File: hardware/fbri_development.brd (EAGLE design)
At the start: 95 parts, among them IC3 TLV70033DCK, J1 AAA_HOLDER, U1 SAM_D20E, U2 SI4060, U3 MAX1947, U4 ANTENOVA_GPS_M10382, U5 S25FS-S, U6 STM32F_48PIN, Y1 8MHz

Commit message: Before trying Direct Tie Tx/Rx
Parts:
- removed J1: AAA_HOLDER, fbri:AAA
- added C19: 4.7µF, resistor:C0603K
- added C27, C28, C29, C30: 10µF, resistor:C0603K
- added C31, C32: 100pF, resistor:C0603K
- added IC1: (no value), SparkFun:SOT223
- added JP16: (no value), SparkFun:1X02_LOCK
- added R22, R23: 1Ω, microbuilder_v3:_0402
- added U$99: INA216, fbri:WCSP-4
- added U7: LP38501TS-ADJ/NOPB, LP38501TS-ADJ:TO170P1435X457-6N
- moved JP14 70.4 mm to (45.5, 38.5), turned to 180 degrees
- moved JP13 64.4 mm to (45.5, 35.5), turned to 180 degrees
- moved JP12 25.8 mm to (45.6, 15.4), turned to 180 degrees
- moved C14 22.8 mm to (44.0, 23.4)
- moved C4 22.8 mm to (44.0, 26.5)
- moved C5 22.8 mm to (44.0, 24.6)
- moved JP2 22.5 mm to (38.5, 27.0)
- moved L1 22.5 mm to (41.1, 24.1)
- moved R5 22.5 mm to (43.5, 20.0)
- moved R6 22.5 mm to (43.5, 19.0)
- moved R7 22.5 mm to (39.5, 29.0)
- moved R8 22.5 mm to (39.5, 30.0)
- moved U$2 22.5 mm to (43.5, 21.0)
- moved U$5 22.5 mm to (39.5, 31.0)
- moved U3 22.5 mm to (41.1, 21.4)
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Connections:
- removed net N$1: U6.10
- removed net N$5: JP1.2, JP13.1, JP14.1, R5.2, R6.2, U$2.A1
- removed net PWR_BR: U6.19
- new net 1.2VREG_OUT: C27.1, IC1.2, IC1.4, JP16.2
- new net ADJ_REG_EN: U6.13, U7.1
- new net ADJ_REG_OUT: C29.1, C30.1, C32.1, JP13.2, U7.4
- new net ADJ_REG_SWITCHING: U6.14, U7.5
- new net I_PA: U$99.B2
- new net I_STEPUP_IN: U$2.B2, U6.16
- new net I_STEPUP_OUT: U$5.B2, U6.19
- new net I_VDD_GPS: U$62.B2, U6.15
- new net I_VDD_MEM: U$48.B2, U6.12
- new net I_VDD_RADIO: U$60.B2, U6.10
- new net I_VDD_SAMD20: U$30.B2, U6.11
- new net VDD_PA: L2.2, R22.1, R23.1, U$99.A2
- new net VDD_STEPUP: JP1.2, JP13.1, JP14.1, JP16.1, R5.2, R6.2, U$2.A1, U6.17
- net 1.2V: no longer J1.+2, JP13.2
- net 1.8V: now also U6.18
- net 3.3V: now also JP14.2; no longer U6.41
- net 5.0V: now also C19.1, C28.1, C31.1, IC1.3, U7.2
- net GND: now also C19.2, C27.2, C28.2, C29.2, C30.2, C31.2, C32.2, IC1.1, U$99.B1, U7.3, U7.6; no longer J1.-1, J1.-2
- net RADIO_VDD: now also R22.2, R23.2, U$99.A1; no longer L2.2
- net RESETN: now also U1.5; no longer U1.15, U1.6
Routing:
- net 1.8V: track 20.4 -> 98.8 mm, vias 0 -> 2
- net 5.0V: track 11.9 -> 81.7 mm
- net I_VDD_RADIO: track 0.00 -> 45.5 mm, vias 0 -> 4
- net VDD_STEPUP: track 0.00 -> 40.1 mm, vias 0 -> 2
- net I_VDD_SAMD20: track 0.00 -> 36.5 mm, vias 0 -> 2
- net ADJ_REG_OUT: track 0.00 -> 35.4 mm, vias 0 -> 1
- net ADJ_REG_EN: track 0.00 -> 35.1 mm
- net ADJ_REG_SWITCHING: track 0.00 -> 28.8 mm
- net RESETN: track 15.9 -> 36.7 mm, vias 0 -> 2
- net TIME_1KHZ: track 6.47 -> 26.9 mm, vias 0 -> 2
- net I_STEPUP_IN: track 0.00 -> 20.2 mm, vias 0 -> 2
- net I_VDD_MEM: track 0.00 -> 16.9 mm
- net I_VDD_GPS: track 0.00 -> 15.2 mm, vias 0 -> 2
- net 1.2VREG_OUT: track 0.00 -> 14.8 mm
- net SWDCLK: track 20.0 -> 6.06 mm
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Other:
- board outline added: 50 x 50 mm
- board text added: "!IRQ"
- board text added: "!SEL"
- board text added: "Board"
- board text added: "Devlopment"
- board text added: "GPS UART"
- board text added: "HFCLK"
- board text added: "Radio SPI"
- board text removed: "HF_CLK"
- board text removed: "NIRQ"
- board text removed: "NSEL"

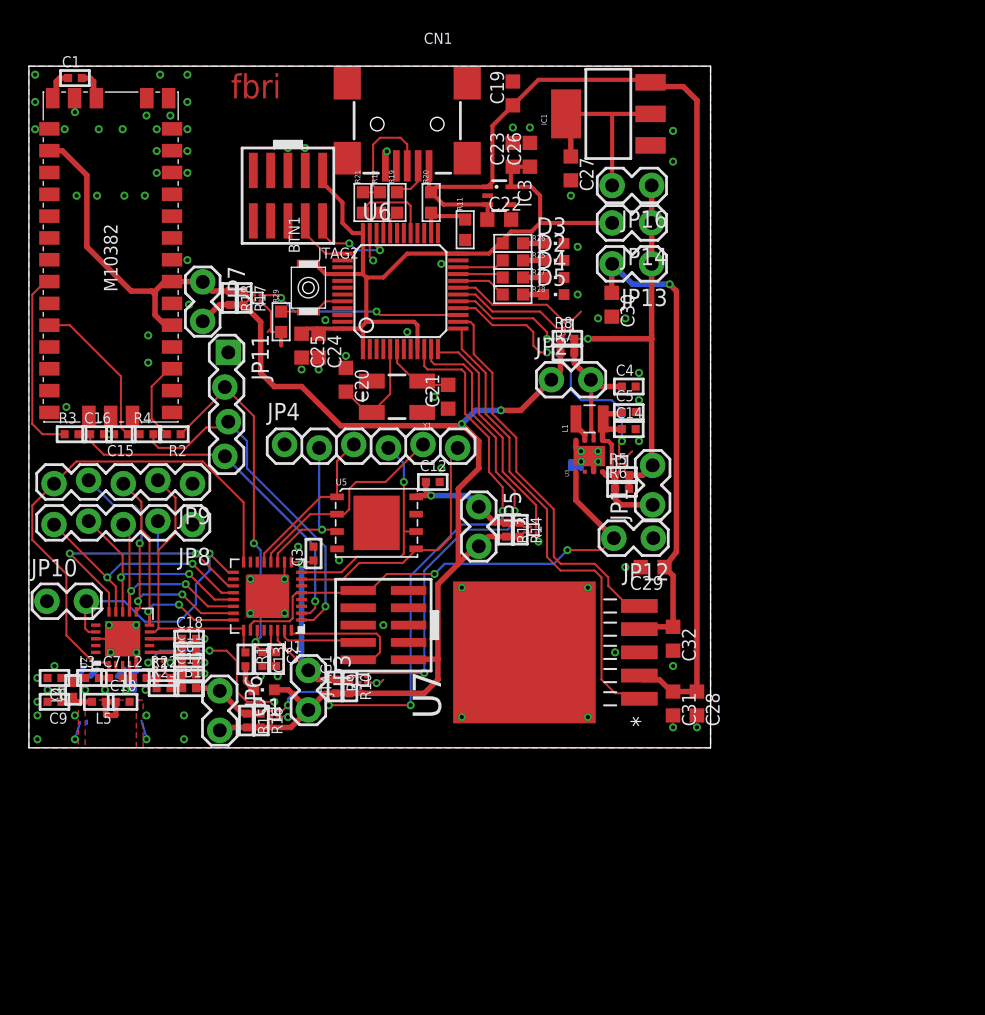
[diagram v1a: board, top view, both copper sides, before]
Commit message: Nearly there, about to re-work MAX1947
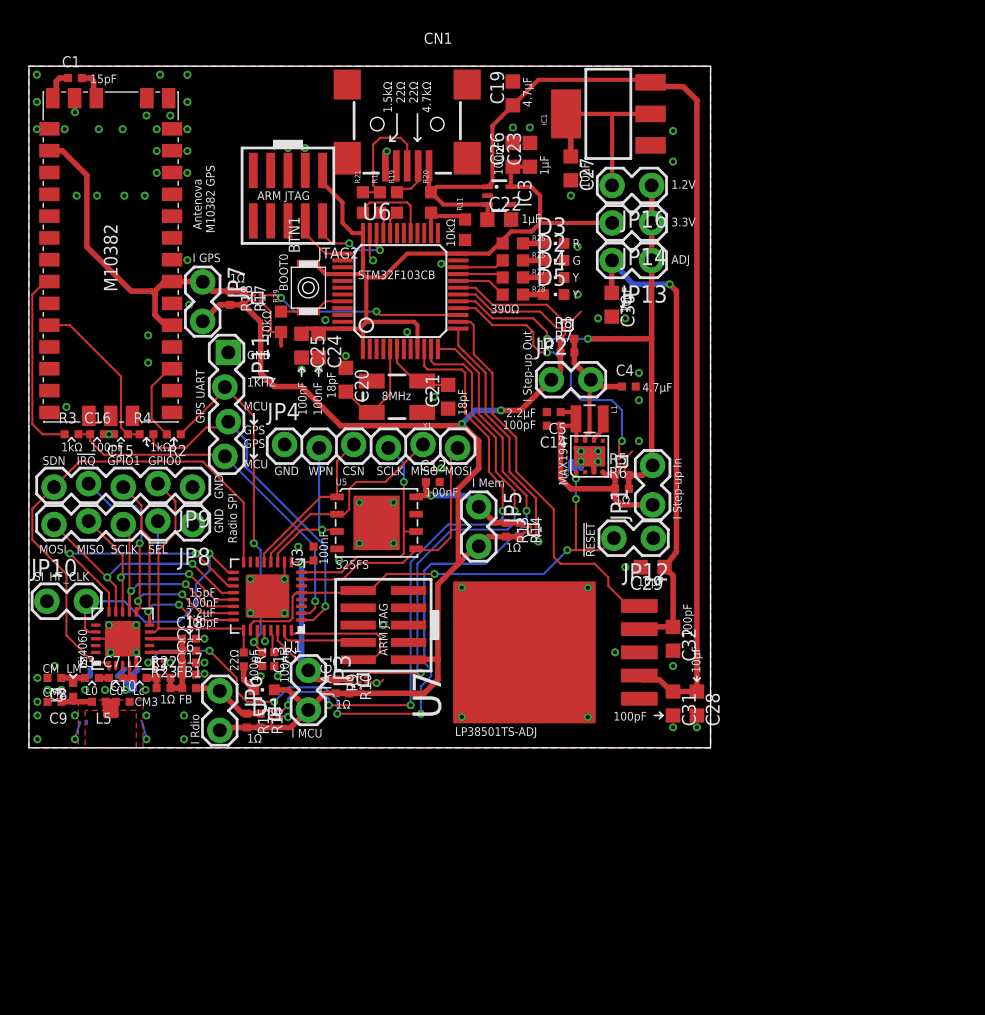
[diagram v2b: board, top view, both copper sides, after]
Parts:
- moved C14 5.51 mm to (38.5, 23.6), turned to 180 degrees
- moved C5 5.50 mm to (38.5, 24.6), turned to 180 degrees
- moved C23 1.25 mm to (36.8, 43.5)
- moved C26 1.25 mm to (35.5, 43.5)
- moved JP13 0.25 mm to (45.5, 35.8)
- moved JP9 0.25 mm to (12.0, 19.2)
- moved C2 0.12 mm to (18.0, 6.50)
- moved R1 0.12 mm to (15.8, 6.49)
- turned L1 to 270 degrees
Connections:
- net ADJ_REG_EN: no longer U6.13
- net GND: now also U3.5; no longer U3.8
- net I_PA: now also U6.12
- net I_VDD_MEM: now also U6.13; no longer U6.12
- net LX: now also U3.6; no longer U3.7
- net STEPUP_IN: now also U3.8; no longer U3.5
- net STEPUP_OUT: now also U3.7; no longer U3.6
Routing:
- net I_PA: track 13.2 -> 61.2 mm, vias 3 -> 6
- net ADJ_REG_EN: track 35.1 -> 0.00 mm
- net STEPUP_IN: track 15.3 -> 19.5 mm
- net ANT: track 3.23 -> 5.20 mm
- net GND: track 36.8 -> 35.0 mm, vias 102 -> 107
- net I_VDD_SAMD20: track 36.5 -> 37.2 mm
- net I_VDD_RADIO: track 45.5 -> 46.1 mm
- net RESETN: track 36.7 -> 36.4 mm, vias 2 -> 4
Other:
- board text added: "(C) Richard Meadows 2014 Version 0.45.0"
- board text added: "1.2V"
- board text added: "1.5kΩ 22Ω 22Ω 4.7kΩ"
- board text added: "100nF"
- board text added: "100pF"
- board text added: "10kΩ"
- board text added: "10µF"
- board text added: "15pF"
- board text added: "15pF 100nF 2.2µF 100pF"
- board text added: "18pF"
- board text added: "1kΩ"
- board text added: "1µF"
- board text added: "1Ω"
- board text added: "2.2µF"
- board text added: "22Ω"
- board text added: "3.3V"
- board text added: "390Ω"
- board text added: "4.7µF"
- board text added: "8MHz"
- board text added: "ADJ"
- board text added: "ARM JTAG"
- board text added: "Antenova M10382 GPS"
- board text added: "BOOT0"
- board text added: "Bristol"
- board text added: "C0"
- board text added: "CM"
- board text added: "CM2"
- board text added: "CM3"
- board text added: "FB"
- board text added: "G"
- board text added: "I GPS"
- board text added: "I MCU"
- board text added: "I Mem"
- board text added: "I Rdio"
- board text added: "I Step-up In"
- board text added: "I Step-up Out"
- board text added: "L0"
- board text added: "LM"
- board text added: "LP38501TS-ADJ"
- board text added: "Lc"
- board text added: "Longshot"
- board text added: "MAX1947"
- board text added: "R"
- board text added: "S25FS"
- board text added: "SI_HF_CLK"
- board text added: "STM32F103CB"
- board text added: "XxXxXxXxXxXx"
- board text added: "Y"
- board text removed: "fbri"

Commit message: Before rename
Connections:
- net SI_HF_CLK: now also U1.18; no longer U1.17
- net SI_SDN: now also U1.17; no longer U1.16
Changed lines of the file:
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@@
 <wire x1="12.25" y1="14.25" x2="9.46" y2="14.25" width="0.1524" layer="16"/>
 <wire x1="9.46" y1="14.25" x2="3" y2="14.25" width="0.1524" layer="16"/>
-<wire x1="15" y1="11.875" x2="14.625" y2="11.875" width="0.1524" layer="1"/>
-<wire x1="14.625" y1="11.875" x2="12.25" y2="14.25" width="0.1524" layer="1"/>
+<wire x1="15" y1="11.875" x2="14.375" y2="11.875" width="0.1524" layer="1"/>
+<wire x1="14.375" y1="11.875" x2="12.625" y2="13.625" width="0.1524" layer="1"/>
+<wire x1="12.625" y1="13.625" x2="12.625" y2="13.875" width="0.1524" layer="1"/>
+<wire x1="12.625" y1="13.875" x2="12.25" y2="14.25" width="0.1524" layer="1"/>
 </signal>
 <signal name="TIME_1KHZ">
@@
 <signal name="SI_HF_CLK">
 <contactref element="U2" pad="17"/>
-<contactref element="U1" pad="17"/>
 <contactref element="JP10" pad="2"/>
 <wire x1="4.905" y1="8.5" x2="4.375" y2="8.5" width="0.1524" layer="1"/>
@@
 <wire x1="12.25" y1="12" x2="13.25" y2="13" width="0.1524" layer="16"/>
 <wire x1="13.25" y1="13" x2="13.25" y2="14.25" width="0.1524" layer="16"/>
-<wire x1="15" y1="12.875" x2="14.625" y2="12.875" width="0.1524" layer="1"/>
-<wire x1="14.625" y1="12.875" x2="13.25" y2="14.25" width="0.1524" layer="1"/>
+<wire x1="14.625" y1="12.375" x2="13.5" y2="13.5" width="0.1524" layer="1"/>
+<wire x1="13.5" y1="13.5" x2="13.5" y2="14" width="0.1524" layer="1"/>
+<wire x1="13.5" y1="14" x2="13.25" y2="14.25" width="0.1524" layer="1"/>
+<contactref element="U1" pad="18"/>
+<wire x1="15" y1="12.375" x2="14.625" y2="12.375" width="0.1524" layer="1"/>
 </signal>
 <signal name="SI_SDN">
-<contactref element="U1" pad="16"/>
 <contactref element="U2" pad="1"/>
 <contactref element="JP9" pad="5"/>
@@
 <wire x1="0.25" y1="15.25" x2="0.25" y2="17.533" width="0.1524" layer="1"/>
 <wire x1="0.25" y1="17.533" x2="1.84" y2="19.123" width="0.1524" layer="1"/>
-<wire x1="15.75" y1="13.625" x2="15.75" y2="18" width="0.1524" layer="1"/>
 <wire x1="12.75" y1="21" x2="3.717" y2="21" width="0.1524" layer="1"/>
 <wire x1="3.717" y1="21" x2="1.84" y2="19.123" width="0.1524" layer="1"/>
-<wire x1="12.75" y1="21" x2="15.75" y2="18" width="0.1524" layer="1"/>
+<wire x1="12.75" y1="21" x2="15" y2="18.75" width="0.1524" layer="1"/>
+<contactref element="U1" pad="17"/>
+<wire x1="15" y1="12.875" x2="15" y2="18.75" width="0.1524" layer="1"/>
 </signal>
 <signal name="SI_GPIO0">
